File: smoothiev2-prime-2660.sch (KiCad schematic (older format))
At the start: 144 parts, among them J1 USB_B, J10 Conn_01x02, J15 Conn_01x02, J2 USB_A, J3 Micro_SD_Card_Det, J30 Conn_01x03_Male, J41 Conn_ARM_JTAG_SWD_10, J42 Conn_01x02, J43 Conn_01x02, J5 Screw_Terminal_01x04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

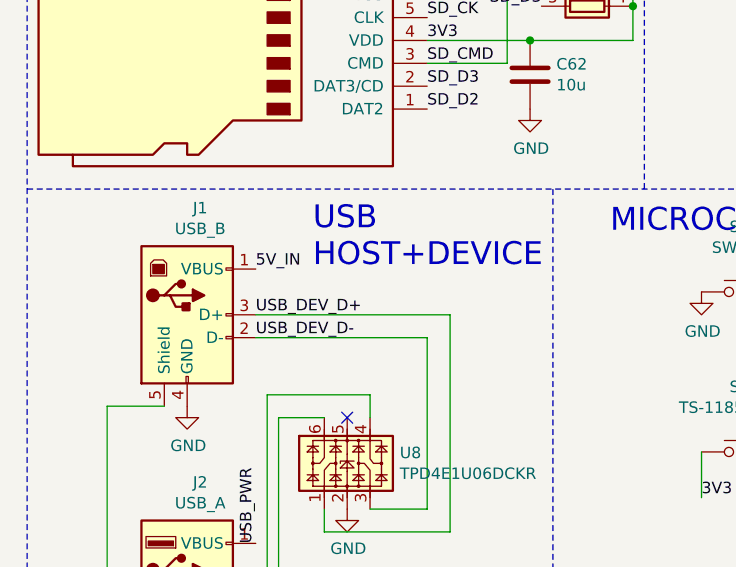
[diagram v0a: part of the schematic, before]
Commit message: Add power monitor circuit to VMOT DC/DC, add disconnect jumper to 5V_IN USB.
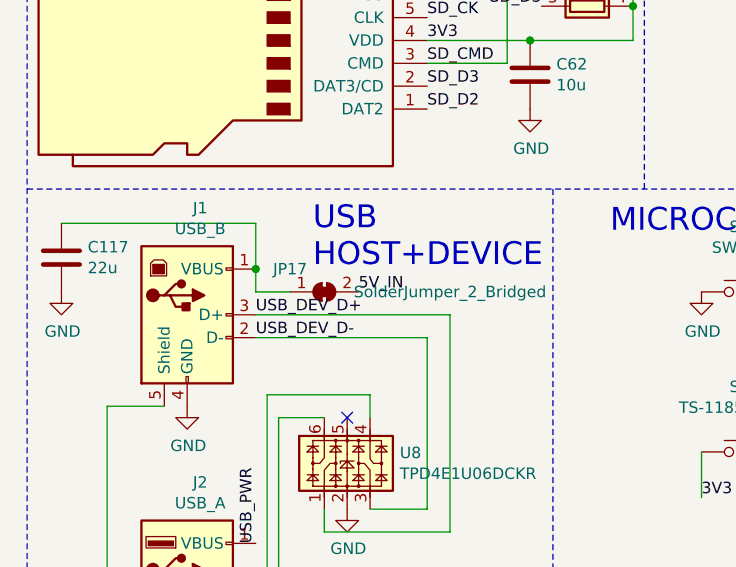
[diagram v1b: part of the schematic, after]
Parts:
- added C117: 22u, Capacitor_SMD:C_0805_2012Metric, symbol Device:C
- added JP17: SolderJumper_2_Bridged, Jumper:SolderJumper-2_P1.3mm_Bridged2Bar_Pad1.0x1.5mm, symbol Jumper:SolderJumper_2_Bridged
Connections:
- net 5V_IN: now also JP17.2 (B); no longer J1.1 (VBUS)
- net GND: now also C117.2
- new net: C117.1, J1.1 (VBUS), JP17.1 (A)
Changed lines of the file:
@@
 Text Label 10450 9050 0    50   ~ 0
 PD15
-Text Label 1500 2450 0    50   ~ 0
+Text Label 1950 2550 0    50   ~ 0
 5V_IN
 Text Label 4650 2750 2    50   ~ 0
@@
 Text Label 9400 1400 0    50   ~ 0
 VLX
+$Comp
+L Device:C C?
+U 1 1 626B4F72
+P 650 2400
+AR Path="/631D7D17/626B4F72" Ref="C?"  Part="1"
+AR Path="/626B4F72" Ref="C117"  Part="1"
+F 0 "C117" H 765 2446 50  0000 L CNN
+F 1 "22u" H 765 2355 50  0000 L CNN
+F 2 "Capacitor_SMD:C_0805_2012Metric" H 688 2250 50  0001 C CNN
+F 3 "~" H 650 2400 50  0001 C CNN
+	1    650  2400
+	1    0    0    -1
+$EndComp
+Wire Wire Line
+	650  2250 1500 2250
+Wire Wire Line
+	1500 2250 1500 2450
+$Comp
+L Jumper:SolderJumper_2_Bridged JP17
+U 1 1 627346A8
+P 1800 2550
+F 0 "JP17" H 1650 2650 50  0000 C CNN
+F 1 "SolderJumper_2_Bridged" H 2350 2550 50  0000 C CNN
+F 2 "Jumper:SolderJumper-2_P1.3mm_Bridged2Bar_Pad1.0x1.5mm" H 1800 2550 50  0001 C CNN
+F 3 "~" H 1800 2550 50  0001 C CNN
+	1    1800 2550
+	1    0    0    -1
+$EndComp
+Wire Wire Line
+	1650 2550 1500 2550
+Wire Wire Line
+	1500 2550 1500 2450
+Connection ~ 1500 2450
+$Comp
+L power:GND #PWR075
+U 1 1 62777716
+P 650 2550
+F 0 "#PWR075" H 650 2300 50  0001 C CNN
+F 1 "GND" H 655 2377 50  0000 C CNN
+F 2 "" H 650 2550 50  0001 C CNN
+F 3 "" H 650 2550 50  0001 C CNN
+	1    650  2550
+	1    0    0    -1
+$EndComp
 $EndSCHEMATC

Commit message: Adapt 2590 board layout to ideal diodes and dual power input connector
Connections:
- net 5V_IN: no longer J42.1 (Pin_1)
- new net 5VPORTIN: J42.1 (Pin_1)
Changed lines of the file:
@@
 $Descr A3 11693 16535 portrait
 encoding utf-8
-Sheet 1 10
+Sheet 1 13
 Title ""
 Date ""
@@
 F8 "3V3_LIM" I L 5250 1350 50
 F9 "VBAT" I L 5250 1450 50
+F10 "5V_PORTIN" I R 5900 700 50
 $EndSheet
 $Comp
@@
 	1    0    0    -1
 $EndComp
-Text Label 7400 1250 0    50   ~ 0
-5V_IN
 $Comp
 L power:GND #PWR034
@@
 	1    0    0    -1
 $EndComp
+Text Label 7400 1250 0    50   ~ 0
+5VPORTIN
+Text Label 5900 700  0    50   ~ 0
+5VPORTIN
 $EndSCHEMATC

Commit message: Updated 2660 version to match 2590 mods.
Updated 2660 version to match 2590 mods.  Ideal diodes, move board thermistor, add extra fet connector, modify probe input.
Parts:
- U2: symbol smoothieparts:STM32H745XIHx -> smoothiev2-prime-2660-rescue:STM32H745XIHx-smoothieparts
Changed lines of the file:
@@
 Connection ~ 5250 12750
 $Comp
-L smoothieparts:STM32H745XIHx U2
+L smoothiev2-prime-2660-rescue:STM32H745XIHx-smoothieparts U2
 U 1 1 607B3889
 P 7550 7450

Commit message: Fix most DRC errors Fix bulk traces for disconnect FET Fix silkscreen indicator for disconnect FET Add fiducials Bump version numbers (proto9 for 2660, proto10 for 2590)
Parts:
- added FID1, FID2, FID3, FID4: Fiducial, Fiducial:Fiducial_0.75mm_Mask1.5mm, symbol Mechanical:Fiducial
- U2: symbol smoothiev2-prime-2660-rescue:STM32H745XIHx-smoothieparts -> smoothieparts:STM32H745XIHx
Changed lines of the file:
@@
 Connection ~ 5250 12750
 $Comp
-L smoothiev2-prime-2660-rescue:STM32H745XIHx-smoothieparts U2
+L smoothieparts:STM32H745XIHx U2
 U 1 1 607B3889
 P 7550 7450
@@
 NoConn ~ 4650 9050
 NoConn ~ 4650 9850
-NoConn ~ 4650 12350
-NoConn ~ 4650 12450
 NoConn ~ 10450 3450
 NoConn ~ 10450 4550
@@
 Text Notes 4100 900  0    50   ~ 0
 Board type 1 - \n2660
-Text Label 9400 2000 1    50   ~ 0
+Text Label 9400 2150 1    50   ~ 0
 VLX
-Wire Wire Line
-	9400 2150 9400 2000
 Text Label 9400 1400 0    50   ~ 0
 VLX
@@
 Text Label 5900 700  0    50   ~ 0
 5VPORTIN
+NoConn ~ 4650 12350
+NoConn ~ 4650 12450
+$Comp
+L Mechanical:Fiducial FID1
+U 1 1 63DA9C6F
+P 9250 14950
+F 0 "FID1" H 9335 14996 50  0000 L CNN
+F 1 "Fiducial" H 9335 14905 50  0000 L CNN
+F 2 "Fiducial:Fiducial_0.75mm_Mask1.5mm" H 9250 14950 50  0001 C CNN
+F 3 "~" H 9250 14950 50  0001 C CNN
+	1    9250 14950
+	1    0    0    -1
+$EndComp
+$Comp
+L Mechanical:Fiducial FID2
+U 1 1 63DAABF5
+P 9250 15150
+F 0 "FID2" H 9335 15196 50  0000 L CNN
+F 1 "Fiducial" H 9335 15105 50  0000 L CNN
+F 2 "Fiducial:Fiducial_0.75mm_Mask1.5mm" H 9250 15150 50  0001 C CNN
+F 3 "~" H 9250 15150 50  0001 C CNN
+	1    9250 15150
+	1    0    0    -1
+$EndComp
+$Comp
+L Mechanical:Fiducial FID3
+U 1 1 63DAB223
+P 9850 14950
+F 0 "FID3" H 9935 14996 50  0000 L CNN
+F 1 "Fiducial" H 9935 14905 50  0000 L CNN
+F 2 "Fiducial:Fiducial_0.75mm_Mask1.5mm" H 9850 14950 50  0001 C CNN
+F 3 "~" H 9850 14950 50  0001 C CNN
+	1    9850 14950
+	1    0    0    -1
+$EndComp
+$Comp
+L Mechanical:Fiducial FID4
+U 1 1 63DAB7DB
+P 9850 15150
+F 0 "FID4" H 9935 15196 50  0000 L CNN
+F 1 "Fiducial" H 9935 15105 50  0000 L CNN
+F 2 "Fiducial:Fiducial_0.75mm_Mask1.5mm" H 9850 15150 50  0001 C CNN
+F 3 "~" H 9850 15150 50  0001 C CNN
+	1    9850 15150
+	1    0    0    -1
+$EndComp
 $EndSCHEMATC
